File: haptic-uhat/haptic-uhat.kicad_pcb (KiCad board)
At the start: 2 copper layers, 65 x 30 mm, 62 parts, among them J1 Conn_01x04_Male, J2 RPi_GPIO, J3 Conn_01x16_Male, U1 TCA9548APW, U10 AZ1117CH-3_3TRG1, U2 DRV2605L, U3 DRV2605L, U4 DRV2605L, U5 DRV2605L, U6 DRV2605L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

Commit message: Adds manufacturing data
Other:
- board text added: "OctoPulse v1 12-10-2019"
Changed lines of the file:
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@@
   (general
     (thickness 1.6)
-    (drawings 17)
+    (drawings 18)
     (tracks 543)
     (zones 0)
@@
       (net 4 +3V3))
   )
+  (gr_text "OctoPulse v1\n12-10-2019" (at 62.23 34.29) (layer F.SilkS)
+    (effects (font (size 1 1) (thickness 0.15)))
+  )
   (gr_line (start 12.5 27.5) (end 12.5 51.5) (layer Edge.Cuts) (width 0.1))

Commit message: Updates hardware to version 2, which corrects backwards SDA/SCL, and adds second button for IP. Original button was wired to the same GPIO that the LiPo board uses to indicate low battery - we can use that for shutdown as well.
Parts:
- added R22: 10K, Resistor_SMD:R_0603_1608Metric, F.Cu at (67.0, 43.8)
- added S2: B3F-1000, digikey-footprints:Switch_Tactile_THT_B3F-1xxx, F.Cu at (69.2, 42.5)
- moved R1 5.41 mm to (69.5, 39.0), turned to 180 degrees
- moved JP1 5.00 mm to (74.0, 39.0)
- moved R2 4.74 mm to (69.5, 36.5), turned to 180 degrees
- moved R3 4.50 mm to (69.5, 34.0), turned to 180 degrees
- moved JP2 3.50 mm to (74.0, 36.5)
- moved JP3 2.00 mm to (74.0, 34.0)
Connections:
- J2 pad 3: /SCL_PI -> /SDA_PI
- J2 pad 37: (no net) -> /IP_BTN
- J2 pad 5: /SDA_PI -> /SCL_PI
- J2 pad 7: /IP_BTN -> /SHDN_BTN
- R21 pad 2: /IP_BTN -> /SHDN_BTN
- S1 pad 3: /IP_BTN -> /SHDN_BTN
- S1 pad 4: /IP_BTN -> /SHDN_BTN
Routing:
- net /SHDN_BTN: track 0.00 -> 26.5 mm
- net +3V3: track 265.7 -> 276.1 mm
- net /SDA_PI: track 24.9 -> 28.8 mm
- net /A0: track 38.5 -> 36.8 mm
- net /A1: track 36.3 -> 35.1 mm
- net /SCL_PI: track 28.8 -> 27.8 mm
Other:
- board text added: "OctoPulse v2 05-11-2019"
- board text added: "Power Off"
- board text added: "Show IP"
- board text removed: "OctoPulse v1 12-10-2019"

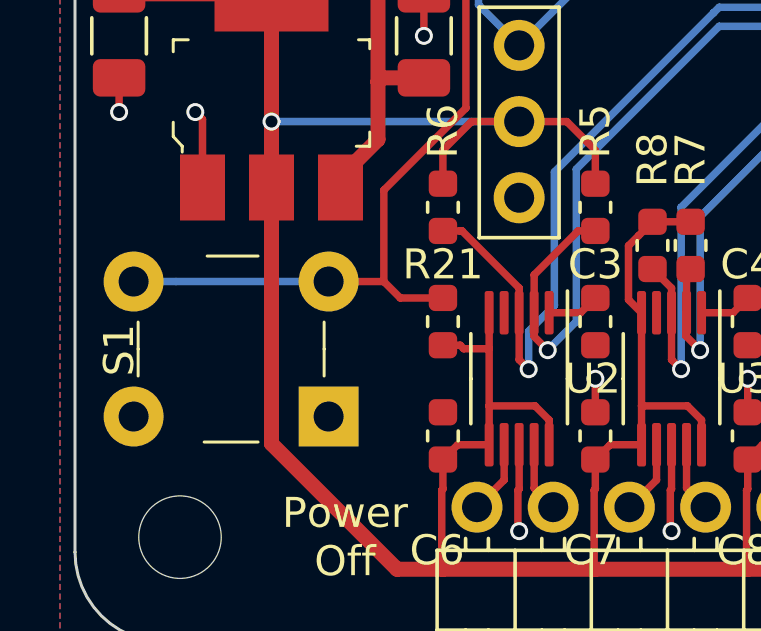
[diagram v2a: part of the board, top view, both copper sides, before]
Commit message: Hey, guess what! The LiPo shim uses active-high on GPIO4 to indicate low battery. Swapped the button around to do the same. That would have been a fun one to debug...
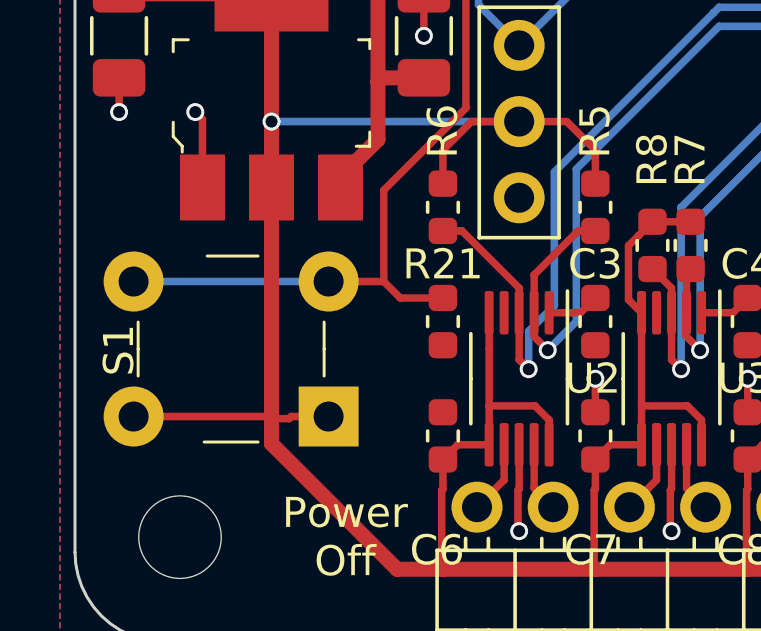
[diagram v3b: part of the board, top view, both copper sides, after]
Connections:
- R21 pad 1: +3V3 -> GND
- S1 pad 1: GND -> +3V3
- S1 pad 2: GND -> +3V3
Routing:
- net +3V3: track 276.1 -> 281.1 mm
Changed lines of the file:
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@@
     (thickness 1.6)
     (drawings 20)
-    (tracks 560)
+    (tracks 563)
     (zones 0)
     (modules 64)
@@
     (add_net /SDA_PI)
     (add_net /SHDN_BTN)
-    (add_net /TRIG0)
-    (add_net /TRIG1)
-    (add_net /TRIG2)
-    (add_net /TRIG3)
-    (add_net /TRIG4)
-    (add_net /TRIG5)
-    (add_net /TRIG6)
-    (add_net /TRIG7)
     (add_net GND)
     (add_net "Net-(C10-Pad1)")
@@
     (add_net "Net-(C5-Pad1)")
     (add_net "Net-(C9-Pad1)")
-    (add_net "Net-(J2-Pad1)")
-    (add_net "Net-(J2-Pad10)")
-    (add_net "Net-(J2-Pad11)")
-    (add_net "Net-(J2-Pad12)")
-    (add_net "Net-(J2-Pad13)")
-    (add_net "Net-(J2-Pad15)")
-    (add_net "Net-(J2-Pad16)")
-    (add_net "Net-(J2-Pad17)")
-    (add_net "Net-(J2-Pad18)")
-    (add_net "Net-(J2-Pad19)")
-    (add_net "Net-(J2-Pad21)")
-    (add_net "Net-(J2-Pad22)")
-    (add_net "Net-(J2-Pad23)")
-    (add_net "Net-(J2-Pad24)")
-    (add_net "Net-(J2-Pad26)")
-    (add_net "Net-(J2-Pad27)")
-    (add_net "Net-(J2-Pad28)")
-    (add_net "Net-(J2-Pad29)")
-    (add_net "Net-(J2-Pad31)")
-    (add_net "Net-(J2-Pad32)")
-    (add_net "Net-(J2-Pad33)")
-    (add_net "Net-(J2-Pad35)")
-    (add_net "Net-(J2-Pad36)")
-    (add_net "Net-(J2-Pad38)")
-    (add_net "Net-(J2-Pad40)")
-    (add_net "Net-(J2-Pad8)")
     (add_net "Net-(R4-Pad2)")
   )
@@
     )
     (pad 1 smd roundrect (at -0.7875 0 90) (size 0.875 0.95) (layers F.Cu F.Paste F.Mask) (roundrect_rratio 0.25)
-      (net 4 +3V3))
+      (net 1 GND))
     (pad 2 smd roundrect (at 0.7875 0 90) (size 0.875 0.95) (layers F.Cu F.Paste F.Mask) (roundrect_rratio 0.25)
       (net 51 /SHDN_BTN))
@@
     (fp_line (start 0.2512 -0.7394) (end 6.2512 -0.7394) (layer F.Fab) (width 0.1))
     (pad 1 thru_hole rect (at 0.0012 0.0106 180) (size 2 2) (drill 1) (layers *.Cu *.Mask)
-      (net 1 GND))
+      (net 4 +3V3))
     (pad 2 thru_hole circle (at 6.5012 0.0106 180) (size 2 2) (drill 1) (layers *.Cu *.Mask)
-      (net 1 GND))
+      (net 4 +3V3))
     (pad 3 thru_hole circle (at 0.0012 4.5106 180) (size 2 2) (drill 1) (layers *.Cu *.Mask)
       (net 51 /SHDN_BTN))
@@
   (segment (start 38.265 35.0775) (end 38.265 33.02) (width 0.25) (layer F.Cu) (net 4))
   (segment (start 38.1 35.2425) (end 38.265 35.0775) (width 0.25) (layer F.Cu) (net 4))
-  (segment (start 25.4575 44.72) (end 26.305 44.72) (width 0.25) (layer F.Cu) (net 4))
-  (segment (start 25.34 44.6025) (end 25.4575 44.72) (width 0.25) (layer F.Cu) (net 4))
-  (segment (start 24.765 44.6025) (end 25.34 44.6025) (width 0.25) (layer F.Cu) (net 4))
   (segment (start 26.305 43.52) (end 26.305 44.72) (width 0.25) (layer F.Cu) (net 4))
   (segment (start 26.305 44.72) (end 26.305 46.625) (width 0.25) (layer F.Cu) (net 4))
@@
   (segment (start 29.845 38.1) (end 28.8925 37.1475) (width 0.25) (layer F.Cu) (net 4))
   (segment (start 23.234398 52.07) (end 24.765 52.07) (width 0.5) (layer F.Cu) (net 4))
-  (segment (start 19.05 39.345) (end 19.05 47.885602) (width 0.5) (layer F.Cu) (net 4))
   (segment (start 19.05 47.885602) (end 23.234398 52.07) (width 0.5) (layer F.Cu) (net 4))
   (segment (start 18.895 32.89) (end 19.05 33.045) (width 0.5) (layer F.Cu) (net 4))
@@
   (segment (start 67 42.425) (end 65.0625 40.4875) (width 0.25) (layer F.Cu) (net 4))
   (segment (start 67 42.9625) (end 67 42.425) (width 0.25) (layer F.Cu) (net 4))
+  (segment (start 19.6332 47.05) (end 19.05 47.05) (width 0.25) (layer F.Cu) (net 4))
+  (segment (start 19.7038 46.9794) (end 19.6332 47.05) (width 0.25) (layer F.Cu) (net 4))
+  (segment (start 20.9538 46.9794) (end 19.7038 46.9794) (width 0.25) (layer F.Cu) (net 4))
+  (segment (start 19.05 39.345) (end 19.05 47.05) (width 0.5) (layer F.Cu) (net 4))
+  (segment (start 19.05 47.05) (end 19.05 47.885602) (width 0.5) (layer F.Cu) (net 4))
+  (segment (start 18.9794 46.9794) (end 19.05 47.05) (width 0.25) (layer F.Cu) (net 4))
+  (segment (start 14.4538 46.9794) (end 18.9794 46.9794) (width 0.25) (layer F.Cu) (net 4))
   (segment (start 29.3525 43.52) (end 29.845 43.0275) (width 0.25) (layer F.Cu) (net 5))
   (segment (start 28.305 43.52) (end 29.3525 43.52) (width 0.25) (layer F.Cu) (net 5))
